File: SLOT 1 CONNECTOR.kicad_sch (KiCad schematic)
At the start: 27 parts

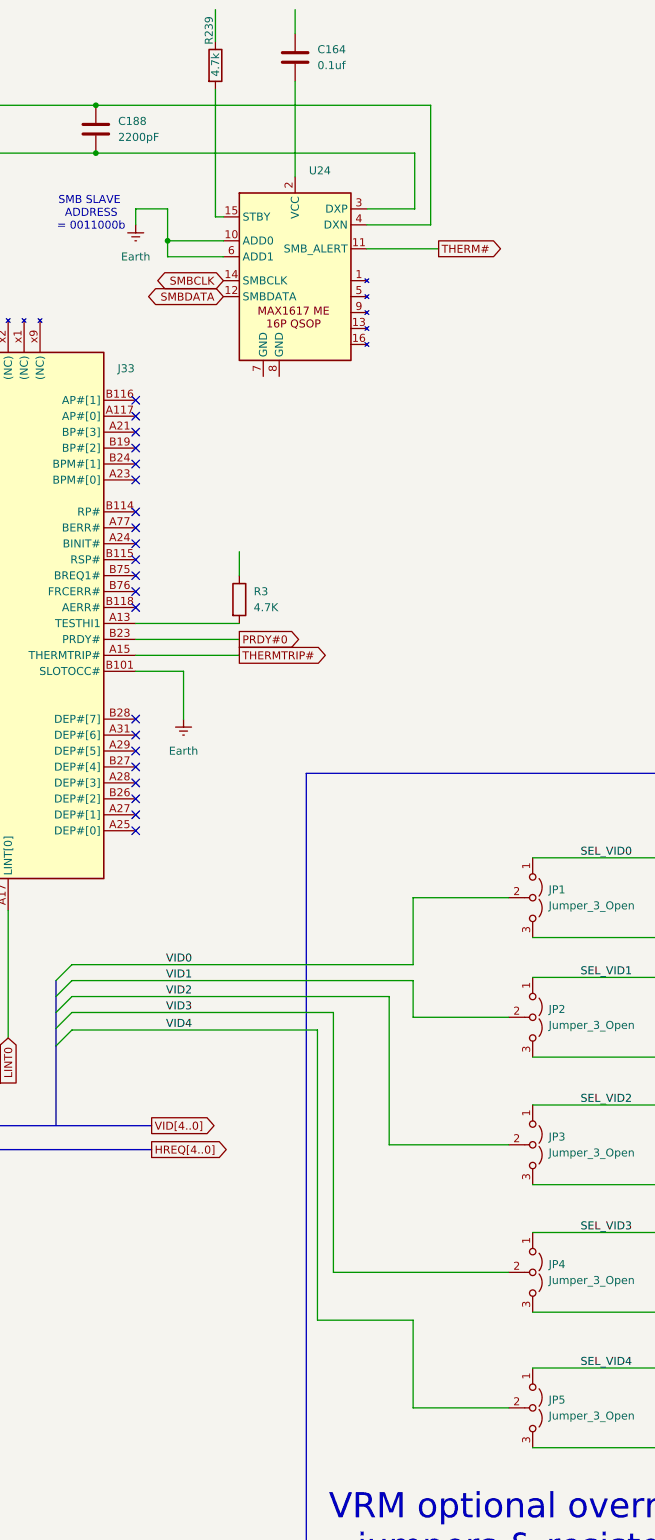
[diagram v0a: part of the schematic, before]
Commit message: improved Cover Sheet, BLOCK DIAGRAM from PDF thru SVG import
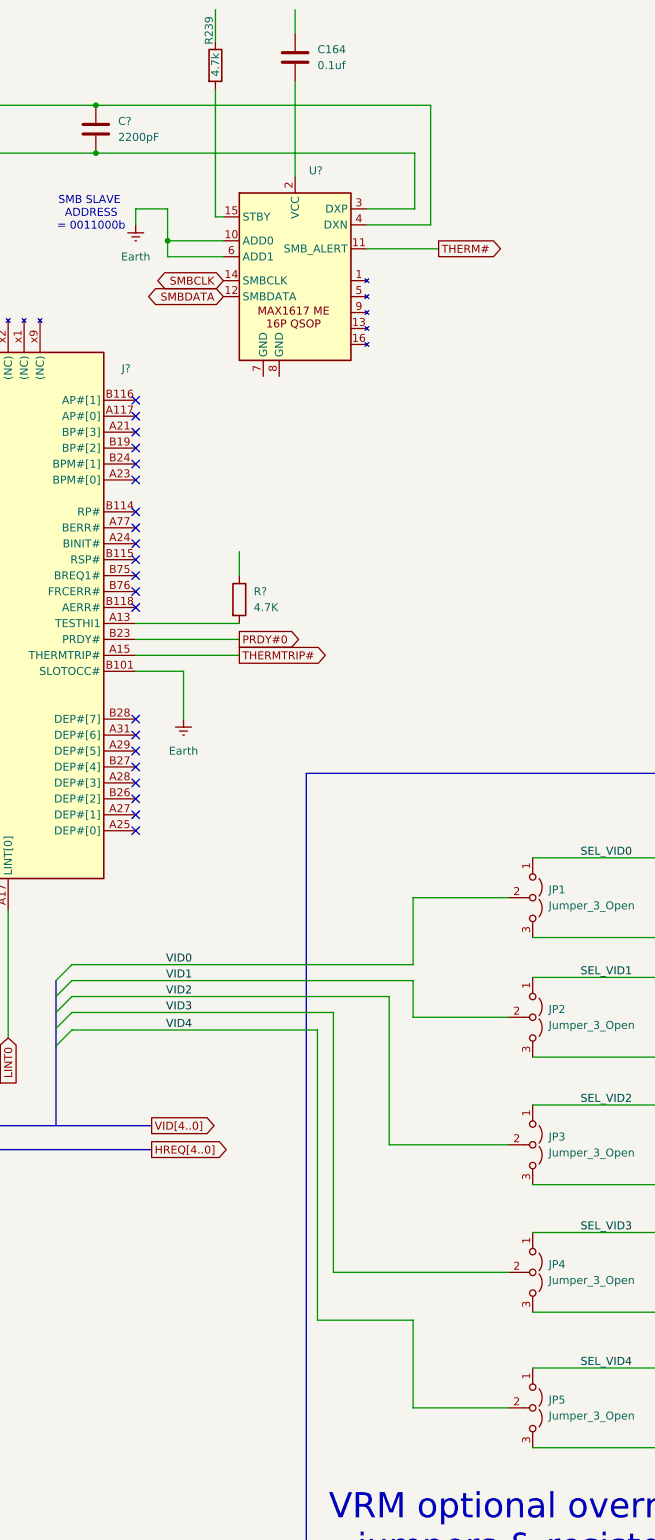
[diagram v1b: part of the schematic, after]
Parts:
- removed C188: 2200pF, Capacitor_SMD:C_0201_0603Metric, symbol Device:C
- removed J33: ~, P2-3_ERA:Slot1_GENERIC, symbol P2-3_era:Slot1_Generic
- removed R3: 4.7K, Resistor_SMD:R_0201_0603Metric, symbol Device:R
- removed U24: ~, Package_SO:QSOP-16_3.9x4.9mm_P0.635mm, symbol P2-3_era:MAX1617_ME
- added C?: 2200pF, Capacitor_SMD:C_0201_0603Metric, symbol Device:C
- added J?: ~, P2-3_ERA:Slot1_GENERIC, symbol P2-3_era:Slot1_Generic
- added R?: 4.7K, Resistor_SMD:R_0201_0603Metric, symbol Device:R
- added U?: ~, Package_SO:QSOP-16_3.9x4.9mm_P0.635mm, symbol P2-3_era:MAX1617_ME
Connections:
- net 100/66#: now also J?.B21 (100/66#)
- net A20M#: now also J?.A05 (A20M#)
- net ADS#: now also J?.A115 (ADS#)
- net BNR#: now also J?.A101 (BNR#)
- net BPRI#: now also J?.A103 (BPRI#)
- net BREQ0#: now also J?.A76 (BREQ0#)
- net CPUHCLK: now also J?.A75 (BCLK)
- net DBSY#: now also J?.A111 (DBSY#)
- net DEFER#: now also J?.A105 (DEFER#)
- net DRDY#: now also J?.B107 (DRDY#)
- net Earth: now also J?.A02 (GND), J?.A06 (GND), J?.A10 (GND), J?.A102 (GND), J?.A106 (GND), J?.A110 (GND), J?.A114 (GND), J?.A118 (GND), J?.A14 (GND), J?.A18 (GND), J?.A22 (GND), J?.A26 (GND), J?.A30 (GND), J?.A34 (GND), J?.A38 (GND), J?.A42 (GND), J?.A46 (GND), J?.A50 (GND), J?.A54 (GND), J?.A58 (GND), J?.A62 (GND), J?.A66 (GND), J?.A70 (GND), J?.A74 (GND), J?.A78 (GND), J?.A82 (GND), J?.A86 (GND), J?.A90 (GND), J?.A94 (GND), J?.A98 (GND), J?.B101 (SLOTOCC#), U?.10 (ADD0), U?.6 (ADD1)
- net FERR#: now also J?.A07 (FERR#)
- net FLUSH#: now also J?.B02 (FLUSH#)
- net HA#10: now also J?.A96 (A#[10])
- net HA#11: now also J?.B92 (A#[11])
- net HA#12: now also J?.B94 (A#[12])
- net HA#13: now also J?.A93 (A#[13])
- net HA#14: now also J?.A95 (A#[14])
- net HA#15: now also J?.B90 (A#[15])
- net HA#16: now also J?.A92 (A#[16])
- net HA#17: now also J?.B91 (A#[17])
- net HA#18: now also J?.A91 (A#[18])
- net HA#19: now also J?.A89 (A#[19])
- net HA#20: now also J?.B86 (A#[20])
- net HA#21: now also J?.B87 (A#[21])
- net HA#22: now also J?.A85 (A#[22])
- net HA#23: now also J?.A87 (A#[23])
- net HA#24: now also J?.B83 (A#[24])
- net HA#25: now also J?.B88 (A#[25])
- net HA#26: now also J?.B82 (A#[26])
- net HA#27: now also J?.A84 (A#[27])
- net HA#28: now also J?.B84 (A#[28])
- net HA#29: now also J?.B80 (A#[29])
- net HA#3: now also J?.B98 (A#[3])
- net HA#30: now also J?.A81 (A#[30])
- net HA#31: now also J?.A83 (A#[31])
- net HA#4: now also J?.A100 (A#[4])
- net HA#5: now also J?.A97 (A#[5])
- net HA#6: now also J?.B99 (A#[6])
- net HA#7: now also J?.B96 (A#[7])
- net HA#8: now also J?.B95 (A#[8])
- net HA#9: now also J?.A99 (A#[9])
- net HD#0: now also J?.B72 (D#[0])
- net HD#1: now also J?.A73 (D#[1])
- net HD#10: now also J?.A65 (D#[10])
- net HD#11: now also J?.A64 (D#[11])
- net HD#12: now also J?.B66 (D#[12])
- net HD#13: now also J?.A63 (D#[13])
- net HD#14: now also J?.A67 (D#[14])
- net HD#15: now also J?.B64 (D#[15])
- net HD#16: now also J?.A61 (D#[16])
- net HD#17: now also J?.B63 (D#[17])
- net HD#18: now also J?.B60 (D#[18])
- net HD#19: now also J?.B59 (D#[19])
- net HD#2: now also J?.B71 (D#[2])
- net HD#20: now also J?.B62 (D#[20])
- net HD#21: now also J?.A60 (D#[21])
- net HD#22: now also J?.B58 (D#[22])
- net HD#23: now also J?.A59 (D#[23])
- net HD#24: now also J?.A57 (D#[24])
- net HD#25: now also J?.B56 (D#[25])
- net HD#26: now also J?.B55 (D#[26])
- net HD#27: now also J?.A56 (D#[27])
- net HD#28: now also J?.B52 (D#[28])
- net HD#29: now also J?.B54 (D#[29])
- net HD#3: now also J?.A72 (D#[3])
- net HD#30: now also J?.A55 (D#[30])
- net HD#31: now also J?.A53 (D#[31])
- net HD#32: now also J?.B51 (D#[32])
- net HD#33: now also J?.A51 (D#[33])
- net HD#34: now also J?.B48 (D#[34])
- net HD#35: now also J?.A52 (D#[35])
- net HD#36: now also J?.B46 (D#[36])
- net HD#37: now also J?.A49 (D#[37])
- net HD#38: now also J?.B50 (D#[38])
- net HD#39: now also J?.A45 (D#[39])
- net HD#4: now also J?.B70 (D#[4])
- net HD#40: now also J?.B47 (D#[40])
- net HD#41: now also J?.B42 (D#[41])
- net HD#42: now also J?.A43 (D#[42])
- net HD#43: now also J?.A48 (D#[43])
- net HD#44: now also J?.B44 (D#[44])
- net HD#45: now also J?.A44 (D#[45])
- net HD#46: now also J?.A39 (D#[46])
- net HD#47: now also J?.B43 (D#[47])
- net HD#48: now also J?.B39 (D#[48])
- net HD#49: now also J?.A40 (D#[49])
- net HD#5: now also J?.A71 (D#[5])
- net HD#50: now also J?.B35 (D#[50])
- net HD#51: now also J?.A41 (D#[51])
- net HD#52: now also J?.B40 (D#[52])
- net HD#53: now also J?.A36 (D#[53])
- net HD#54: now also J?.B36 (D#[54])
- net HD#55: now also J?.A33 (D#[55])
- net HD#56: now also J?.B34 (D#[56])
- net HD#57: now also J?.A37 (D#[57])
- net HD#58: now also J?.B31 (D#[58])
- net HD#59: now also J?.B38 (D#[59])
- net HD#6: now also J?.B68 (D#[6])
- net HD#60: now also J?.A35 (D#[60])
- net HD#61: now also J?.A32 (D#[61])
- net HD#62: now also J?.B30 (D#[62])
- net HD#63: now also J?.B32 (D#[63])
- net HD#7: now also J?.B67 (D#[7])
- net HD#8: now also J?.A69 (D#[8])
- net HD#9: now also J?.A68 (D#[9])
- net HINIT#: now also J?.B04 (INIT#)
- net HIT#: now also J?.B110 (HIT#)
- net HITM#: now also J?.A109 (HITM#)
- net HLOCK#: now also J?.B106 (LOCK#)
- net HRESET#: now also J?.B74 (RESET#)
- net HTRDY#: now also J?.A104 (TRDY#)
- net IGNNE#: now also J?.A08 (IGNNE#)
- net ITPREO#: now also J?.A20 (PREO#)
- net LINT0: now also J?.A17 (LINT[0])
- net LINT1: now also J?.B16 (LINT[1])
- net PICCLK: now also J?.B18 (PICCLK)
- net PICD0: now also J?.A19 (PICD[0])
- net PICD1: now also J?.B22 (PICD[1])
- net PRDY#0: now also J?.B23 (PRDY#)
- net PWRGOOD: now also J?.A12 (PWRGOOD)
- net PX4_SMI#: now also J?.B03 (SMI#)
- net RS#0: now also J?.B108 (RS#[0])
- net RS#1: now also J?.A112 (RS#[1])
- net RS#2: now also J?.B111 (RS#[2])
- net SLP#: now also J?.B08 (SLP#)
- net SMBCLK: now also U?.14 (SMBCLK)
- net SMBDATA: now also U?.12 (SMBDATA)
- net STPCLK#: now also J?.B06 (STPCLK#)
- net TCK: now also J?.B07 (TCK)
- net TDI: now also J?.A09 (TDI)
- net TDO: now also J?.A11 (TDO)
- net THERM#: now also U?.11 (SMB_ALERT)
- net THERMTRIP#: now also J?.A15 (THERMTRIP#)
- net TMS: now also J?.B10 (TMS)
- net TRST#: now also J?.B11 (TRST#)
- net at R222.2: now also J?.A120 (VID[1])
- net at R6.2: now also J?.B41 (EMI)
- net at R239.2: now also U?.15 (STBY)
- net at C164.2: now also U?.2 (VCC)
- net at R223.2: now also J?.A121 (VID[4])
- net at R8.2: now also J?.B100 (EMI)
- net at R219.2: now also J?.B120 (VID[0])
- net at R220.2: now also J?.A119 (VID[2])
- net at R5.2: now also J?.B61 (EMI)
- net at R221.2: now also J?.B119 (VID[3])
- net at R4.2: now also J?.B01 (EMI)
- net at R9.2: now also J?.B81 (EMI)
- new net: C?.2, J?.B14 (RESERVED), U?.3 (DXP)
- new net: C?.1, J?.B15 (RESERVED), U?.4 (DXN)
- new net: J?.A13 (TESTHI1), R?.2
- new net: J?.A01 (VCC_VTT), J?.A03 (VCC_VTT), J?.B05 (VCC_VTT), J?.B09 (VCC_VTT)
- new net: J?.B105 (VCC_CORE), J?.B13 (VCC_CORE), J?.B17 (VCC_CORE), J?.B25 (VCC_CORE), J?.B29 (VCC_CORE), J?.B33 (VCC_CORE), J?.B37 (VCC_CORE), J?.B45 (VCC_CORE), J?.B49 (VCC_CORE), J?.B53 (VCC_CORE), J?.B57 (VCC_CORE), J?.B65 (VCC_CORE), J?.B69 (VCC_CORE), J?.B73 (VCC_CORE), J?.B77 (VCC_CORE), J?.B85 (VCC_CORE), J?.B89 (VCC_CORE), J?.B93 (VCC_CORE), J?.B97 (VCC_CORE)
- new net: J?.B113 (VCC_3), J?.B117 (VCC_3), J?.B121 (VCC_3)
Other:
- title: (none) -> SLOT 1 (PART I)
